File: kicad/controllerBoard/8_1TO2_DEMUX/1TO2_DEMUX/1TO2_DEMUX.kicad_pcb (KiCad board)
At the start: 2 copper layers, 10 parts, among them Q1 PMOS, Q10 NMOS, Q2 PMOS, Q3 NMOS, Q4 NMOS, Q5 PMOS, Q6 PMOS, Q7 NMOS, Q8 NMOS, Q9 PMOS

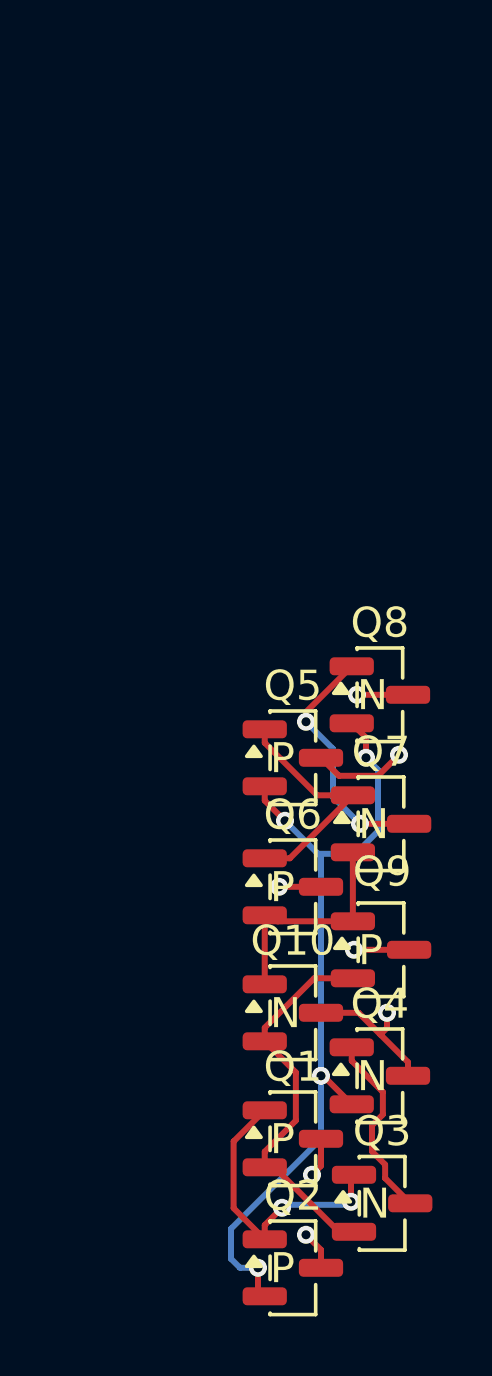
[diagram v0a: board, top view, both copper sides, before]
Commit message: continue routing main controller board
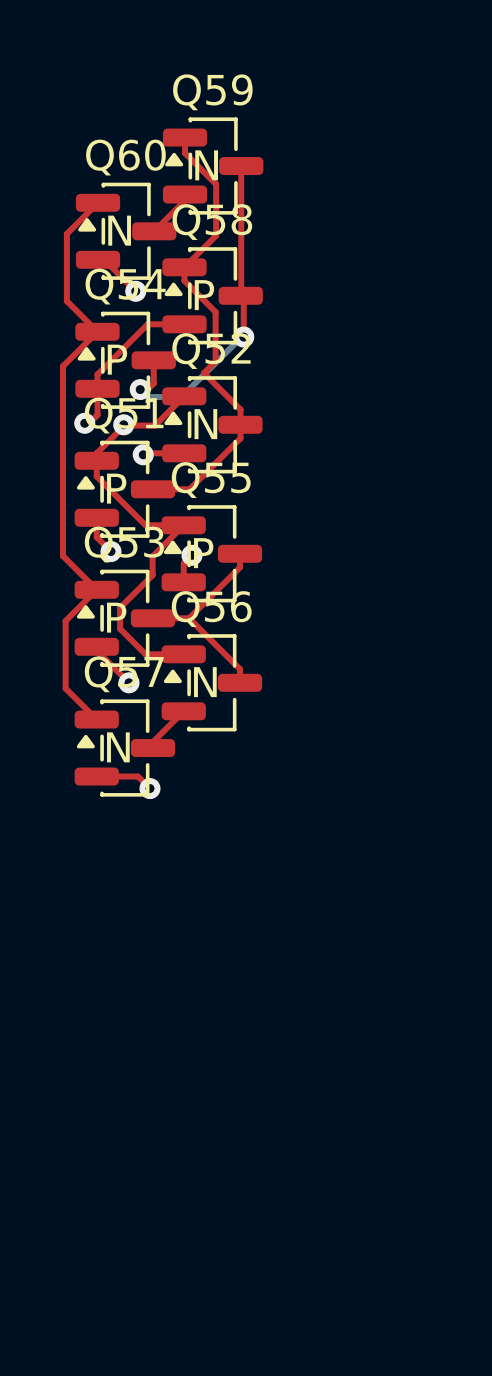
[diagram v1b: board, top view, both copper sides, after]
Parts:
- removed Q1, Q2, Q5, Q6, Q9: PMOS, Package_TO_SOT_SMD:SOT-23-P
- removed Q10, Q3, Q4, Q7, Q8: NMOS, Package_TO_SOT_SMD:SOT-23-N
- added Q51: Q_PMOS_GSD, easyeda2kicad:SOT-23-P, F.Cu at (99.9, 56.2)
- added Q52: Q_NMOS_GSD, easyeda2kicad:SOT-23-N, F.Cu at (102.8, 54.1)
- added Q53: Q_PMOS_GSD, easyeda2kicad:SOT-23-P, F.Cu at (99.9, 60.5)
- added Q54: Q_PMOS_GSD, easyeda2kicad:SOT-23-P, F.Cu at (100.0, 52.0)
- added Q55: Q_PMOS_GSD, easyeda2kicad:SOT-23-P, F.Cu at (102.8, 58.4)
- added Q56: Q_NMOS_GSD, easyeda2kicad:SOT-23-N, F.Cu at (102.8, 62.7)
- added Q57: Q_NMOS_GSD, easyeda2kicad:SOT-23-N, F.Cu at (99.9, 64.9)
- added Q58: Q_PMOS_GSD, easyeda2kicad:SOT-23-P, F.Cu at (102.9, 49.8)
- added Q59: Q_NMOS_GSD, easyeda2kicad:SOT-23-N, F.Cu at (102.9, 45.5)
- added Q60: Q_NMOS_GSD, easyeda2kicad:SOT-23-N, F.Cu at (100.0, 47.6)
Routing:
- net Net-(Q51-D): track 0.00 -> 15.6 mm
- net Net-(Q7-S): track 8.26 -> 0.00 mm, vias 2 -> 0
- net /D: track 27.5 -> 19.9 mm, vias 4 -> 0
- net Net-(Q10-D): track 7.62 -> 0.00 mm
- net Net-(Q3-S): track 6.31 -> 0.00 mm
- net /~{Y_{0}}: track 7.92 -> 11.4 mm, vias 0 -> 2
- net /~{Y_{1}}: track 9.77 -> 6.91 mm, vias 2 -> 0
- net /Addr: track 13.0 -> 14.9 mm, vias 0 -> 1
- net Net-(Q59-S): track 0.00 -> 1.65 mm
- net Net-(Q56-S): track 0.00 -> 1.65 mm
- net GND: track 6.55 -> 5.02 mm, vias 2 -> 3
- net +5V: track 9.01 -> 9.46 mm, vias 5 -> 4
